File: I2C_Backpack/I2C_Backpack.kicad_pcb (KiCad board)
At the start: 2 copper layers, 41.7 x 14.7 mm, 10 parts, among them P1 CONN_01X04, U1 MCP23017_QFN28

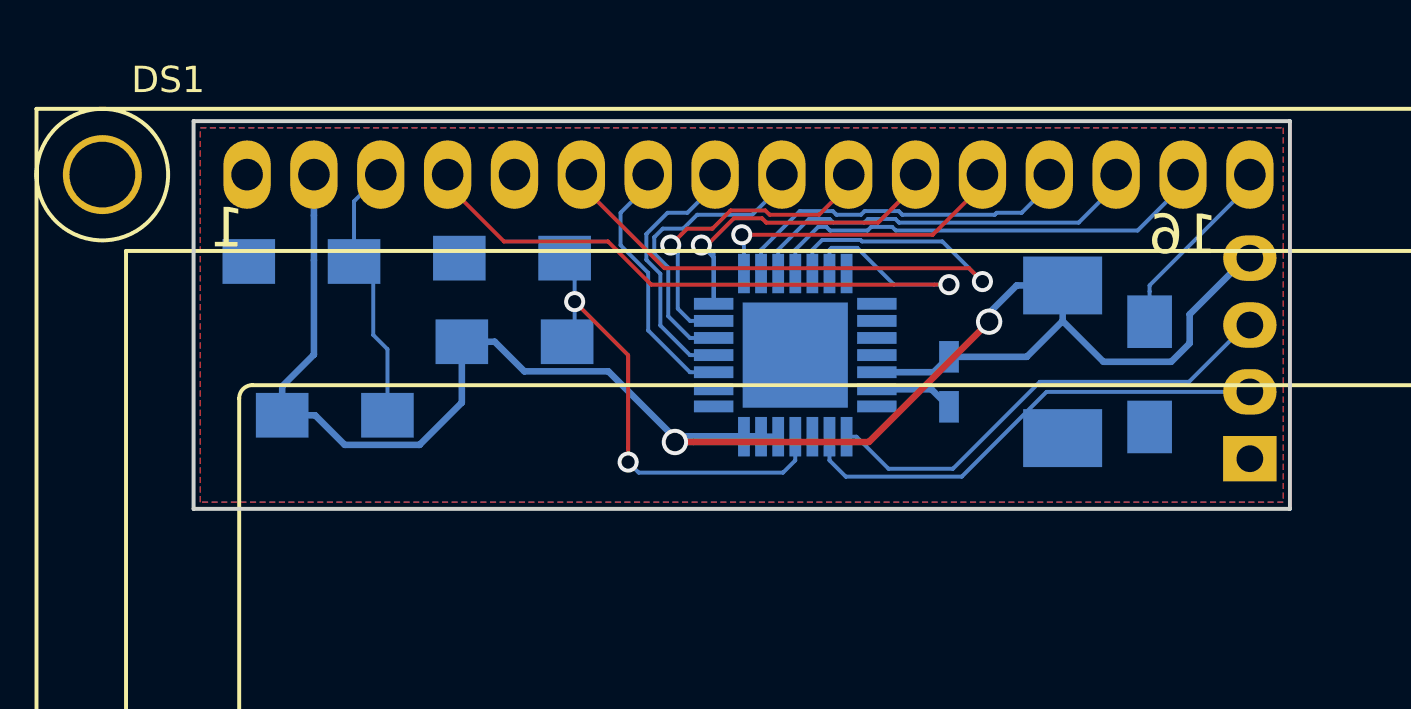
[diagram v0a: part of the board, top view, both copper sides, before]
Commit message: Fixed f*** ups in GND Plane off I2C backpack
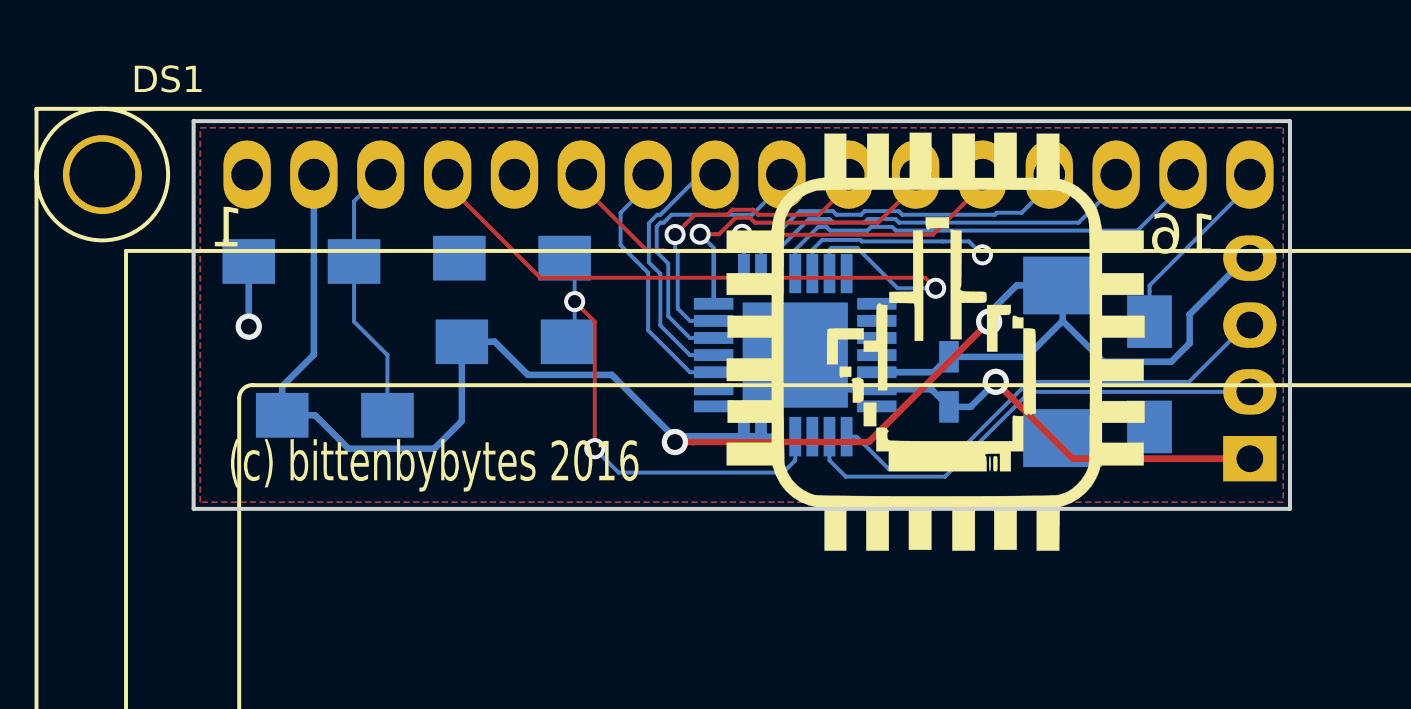
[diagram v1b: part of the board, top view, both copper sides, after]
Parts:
- added G***: LOGO, PIC24 USB:fingerchip_Logo, F.Cu at (170.9, 100.3)
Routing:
- net GND: track 3.02 -> 22.2 mm, vias 0 -> 2
- net /LCD_RS: track 25.7 -> 24.9 mm
- net +5V: track 74.3 -> 74.9 mm
- net /LCD_E: track 27.1 -> 26.6 mm
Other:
- net class POWER: via_drill 0.7 -> 0.6
- board text added: "(c) bittenbybytes 2016"

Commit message: Fixed Enable and RS pin mixupt in LCD backpack
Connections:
- DS1 pad 4: /LCD_E -> /LCD_RS
- DS1 pad 6: /LCD_RS -> /LCD_E
- U1 pad 26: /LCD_RS -> /LCD_E
- U1 pad 27: /LCD_E -> /LCD_RS
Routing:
- net /LCD_RS: track 24.9 -> 26.6 mm
- net /LCD_E: track 26.6 -> 24.9 mm
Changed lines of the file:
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@@
-(kicad_pcb (version 4) (host pcbnew 4.0.2-4+6225~38~ubuntu14.04.1-stable)
+(kicad_pcb (version 4) (host pcbnew 4.0.4+e1-6308~48~ubuntu14.04.1-stable)
   (general
-    (links 0)
+    (links 36)
     (no_connects 0)
     (area 142.672999 91.872999 184.479001 106.755001)
@@
       (net 24 "Net-(U1-Pad28)"))
     (pad 26 smd rect (at -0.65 3.1 180) (size 0.45 1.5) (layers B.Cu B.Paste B.Mask)
+      (net 5 /LCD_E))
+    (pad 27 smd rect (at -1.3 3.1 180) (size 0.45 1.5) (layers B.Cu B.Paste B.Mask)
       (net 4 /LCD_RS))
-    (pad 27 smd rect (at -1.3 3.1 180) (size 0.45 1.5) (layers B.Cu B.Paste B.Mask)
-      (net 5 /LCD_E))
     (pad 20 smd rect (at 3.1 1.3 90) (size 0.45 1.5) (layers B.Cu B.Paste B.Mask)
       (net 18 /D3))
@@
       (net 3 /LCD_VO))
     (pad 4 thru_hole oval (at 7.62 0) (size 1.8 2.6) (drill 1.2) (layers *.Cu *.Mask F.SilkS)
+      (net 4 /LCD_RS))
+    (pad 5 thru_hole oval (at 10.16 0) (size 1.8 2.6) (drill 1.2) (layers *.Cu *.Mask F.SilkS)
+      (net 2 GND))
+    (pad 6 thru_hole oval (at 12.7 0) (size 1.8 2.6) (drill 1.2) (layers *.Cu *.Mask F.SilkS)
       (net 5 /LCD_E))
-    (pad 5 thru_hole oval (at 10.16 0) (size 1.8 2.6) (drill 1.2) (layers *.Cu *.Mask F.SilkS)
-      (net 2 GND))
-    (pad 6 thru_hole oval (at 12.7 0) (size 1.8 2.6) (drill 1.2) (layers *.Cu *.Mask F.SilkS)
-      (net 4 /LCD_RS))
     (pad 7 thru_hole oval (at 15.24 0) (size 1.8 2.6) (drill 1.2) (layers *.Cu *.Mask F.SilkS)
       (net 15 /D0))
@@
   (segment (start 148.844 97.282) (end 148.844 94.996) (width 0.15) (layer B.Cu) (net 3))
   (segment (start 148.844 94.996) (end 149.86 93.98) (width 0.15) (layer B.Cu) (net 3))
-  (segment (start 172.72 97.028) (end 172.566816 96.874816) (width 0.15) (layer F.Cu) (net 4))
-  (segment (start 172.566816 96.874816) (end 161.34917 96.874816) (width 0.15) (layer F.Cu) (net 4))
-  (segment (start 160.73576 96.874816) (end 160.608443 96.874816) (width 0.15) (layer F.Cu) (net 4))
-  (segment (start 159.96128 96.86128) (end 157.48 94.38) (width 0.15) (layer F.Cu) (net 4))
-  (segment (start 161.342466 96.88152) (end 160.742464 96.88152) (width 0.15) (layer F.Cu) (net 4))
-  (segment (start 160.742464 96.88152) (end 160.73576 96.874816) (width 0.15) (layer F.Cu) (net 4))
-  (segment (start 161.34917 96.874816) (end 161.342466 96.88152) (width 0.15) (layer F.Cu) (net 4))
-  (segment (start 160.608443 96.874816) (end 160.594907 96.86128) (width 0.15) (layer F.Cu) (net 4))
-  (segment (start 160.594907 96.86128) (end 159.96128 96.86128) (width 0.15) (layer F.Cu) (net 4))
-  (segment (start 157.48 94.38) (end 157.48 93.98) (width 0.15) (layer F.Cu) (net 4))
-  (segment (start 172.212 96.52) (end 172.72 97.028) (width 0.15) (layer B.Cu) (net 4))
-  (via (at 172.72 97.028) (size 0.8) (drill 0.5) (layers F.Cu B.Cu) (net 4))
-  (segment (start 171.196 96.52) (end 172.212 96.52) (width 0.15) (layer B.Cu) (net 4))
-  (segment (start 168.144281 96.52) (end 171.196 96.52) (width 0.15) (layer B.Cu) (net 4))
-  (segment (start 168.087269 96.462988) (end 168.144281 96.52) (width 0.15) (layer B.Cu) (net 4))
-  (segment (start 166.258 97.738) (end 166.258 96.838) (width 0.15) (layer B.Cu) (net 4))
-  (segment (start 166.258 96.838) (end 166.633012 96.462988) (width 0.15) (layer B.Cu) (net 4))
-  (segment (start 166.633012 96.462988) (end 168.087269 96.462988) (width 0.15) (layer B.Cu) (net 4))
-  (segment (start 157.48 94.38) (end 157.48 93.98) (width 0.15) (layer B.Cu) (net 4))
-  (segment (start 169.498002 98.298) (end 170.376315 98.298) (width 0.15) (layer B.Cu) (net 5))
-  (segment (start 166.908 96.838) (end 166.983001 96.762999) (width 0.15) (layer B.Cu) (net 5))
-  (segment (start 170.376315 98.298) (end 170.942 98.298) (width 0.15) (layer B.Cu) (net 5))
-  (segment (start 170.542001 97.898001) (end 170.942 98.298) (width 0.15) (layer F.Cu) (net 5))
-  (segment (start 152.4 94.38) (end 155.918001 97.898001) (width 0.15) (layer F.Cu) (net 5))
-  (segment (start 166.983001 96.762999) (end 167.963001 96.762999) (width 0.15) (layer B.Cu) (net 5))
-  (segment (start 152.4 93.98) (end 152.4 94.38) (width 0.15) (layer F.Cu) (net 5))
-  (segment (start 166.908 97.738) (end 166.908 96.838) (width 0.15) (layer B.Cu) (net 5))
-  (segment (start 155.918001 97.898001) (end 170.542001 97.898001) (width 0.15) (layer F.Cu) (net 5))
-  (segment (start 167.963001 96.762999) (end 169.498002 98.298) (width 0.15) (layer B.Cu) (net 5))
-  (via (at 170.942 98.298) (size 0.8) (drill 0.5) (layers F.Cu B.Cu) (net 5))
-  (segment (start 152.4 93.58) (end 152.4 93.98) (width 0.15) (layer F.Cu) (net 5))
+  (segment (start 169.498002 98.298) (end 170.376315 98.298) (width 0.15) (layer B.Cu) (net 4))
+  (segment (start 166.908 96.838) (end 166.983001 96.762999) (width 0.15) (layer B.Cu) (net 4))
+  (segment (start 170.376315 98.298) (end 170.942 98.298) (width 0.15) (layer B.Cu) (net 4))
+  (segment (start 170.542001 97.898001) (end 170.942 98.298) (width 0.15) (layer F.Cu) (net 4))
+  (segment (start 152.4 94.38) (end 155.918001 97.898001) (width 0.15) (layer F.Cu) (net 4))
+  (segment (start 166.983001 96.762999) (end 167.963001 96.762999) (width 0.15) (layer B.Cu) (net 4))
+  (segment (start 152.4 93.98) (end 152.4 94.38) (width 0.15) (layer F.Cu) (net 4))
+  (segment (start 166.908 97.738) (end 166.908 96.838) (width 0.15) (layer B.Cu) (net 4))
+  (segment (start 155.918001 97.898001) (end 170.542001 97.898001) (width 0.15) (layer F.Cu) (net 4))
+  (segment (start 167.963001 96.762999) (end 169.498002 98.298) (width 0.15) (layer B.Cu) (net 4))
+  (via (at 170.942 98.298) (size 0.8) (drill 0.5) (layers F.Cu B.Cu) (net 4))
+  (segment (start 152.4 93.58) (end 152.4 93.98) (width 0.15) (layer F.Cu) (net 4))
+  (segment (start 172.72 97.028) (end 172.566816 96.874816) (width 0.15) (layer F.Cu) (net 5))
+  (segment (start 172.566816 96.874816) (end 161.34917 96.874816) (width 0.15) (layer F.Cu) (net 5))
+  (segment (start 160.73576 96.874816) (end 160.608443 96.874816) (width 0.15) (layer F.Cu) (net 5))
+  (segment (start 159.96128 96.86128) (end 157.48 94.38) (width 0.15) (layer F.Cu) (net 5))
+  (segment (start 161.342466 96.88152) (end 160.742464 96.88152) (width 0.15) (layer F.Cu) (net 5))
+  (segment (start 160.742464 96.88152) (end 160.73576 96.874816) (width 0.15) (layer F.Cu) (net 5))
+  (segment (start 161.34917 96.874816) (end 161.342466 96.88152) (width 0.15) (layer F.Cu) (net 5))
+  (segment (start 160.608443 96.874816) (end 160.594907 96.86128) (width 0.15) (layer F.Cu) (net 5))
+  (segment (start 160.594907 96.86128) (end 159.96128 96.86128) (width 0.15) (layer F.Cu) (net 5))
+  (segment (start 157.48 94.38) (end 157.48 93.98) (width 0.15) (layer F.Cu) (net 5))
+  (segment (start 172.212 96.52) (end 172.72 97.028) (width 0.15) (layer B.Cu) (net 5))
+  (via (at 172.72 97.028) (size 0.8) (drill 0.5) (layers F.Cu B.Cu) (net 5))
+  (segment (start 171.196 96.52) (end 172.212 96.52) (width 0.15) (layer B.Cu) (net 5))
+  (segment (start 168.144281 96.52) (end 171.196 96.52) (width 0.15) (layer B.Cu) (net 5))
+  (segment (start 168.087269 96.462988) (end 168.144281 96.52) (width 0.15) (layer B.Cu) (net 5))
+  (segment (start 166.258 97.738) (end 166.258 96.838) (width 0.15) (layer B.Cu) (net 5))
+  (segment (start 166.258 96.838) (end 166.633012 96.462988) (width 0.15) (layer B.Cu) (net 5))
+  (segment (start 166.633012 96.462988) (end 168.087269 96.462988) (width 0.15) (layer B.Cu) (net 5))
+  (segment (start 157.48 94.38) (end 157.48 93.98) (width 0.15) (layer B.Cu) (net 5))
   (segment (start 182.88 93.98) (end 182.88 94.38) (width 0.15) (layer B.Cu) (net 6))
   (segment (start 182.88 94.38) (end 179.07 98.19) (width 0.15) (layer B.Cu) (net 6))
